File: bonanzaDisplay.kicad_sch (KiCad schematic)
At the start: 73 parts, among them J1 OLED-1.31-SSD1322, J15 SWD, J5 Conn_01x10, J6 USB_C_Receptacle_USB2.0, SW1 TS-1088-AR02016, SW2 TS-1088-AR02016, SW4 7*7*5-6P WX, U1 RP2354A, U10 TPS82130, U2 XC6206P302MR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

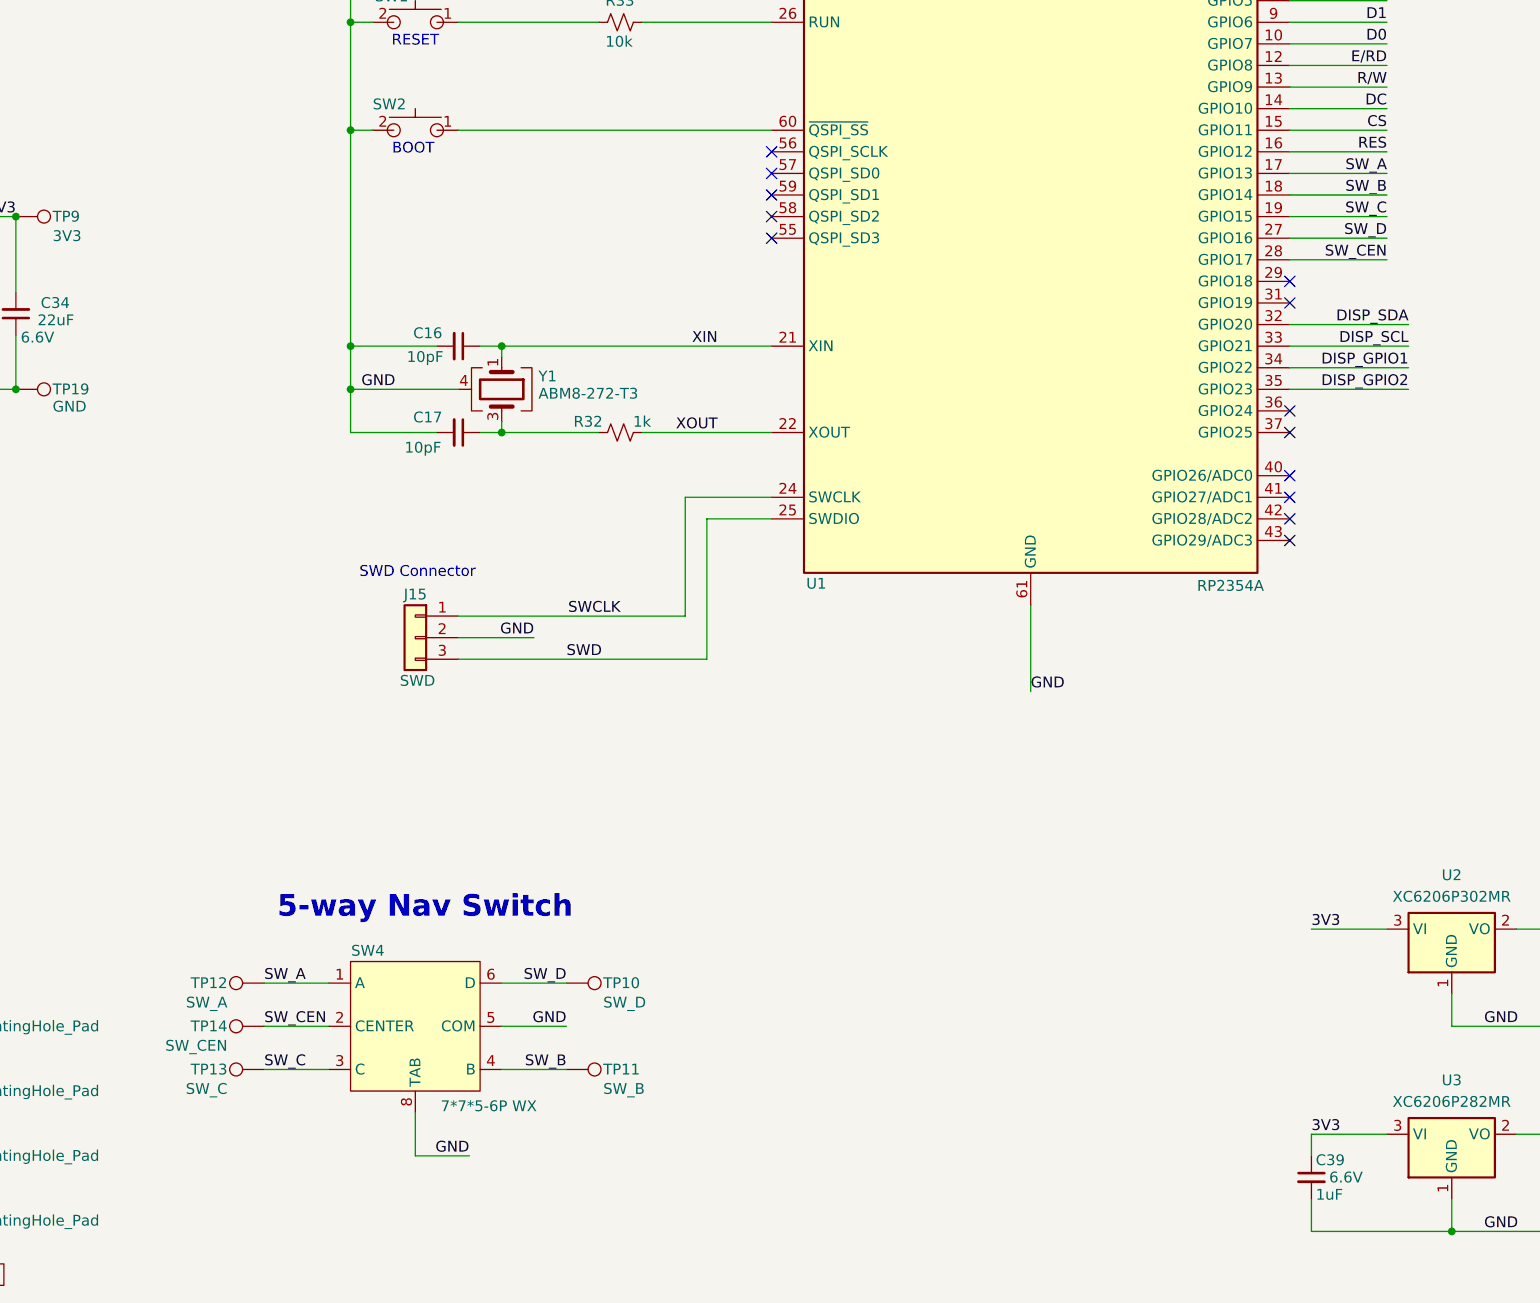
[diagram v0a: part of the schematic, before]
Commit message: switched to dial switch. added OLED 3D CAD. ordered PCBA
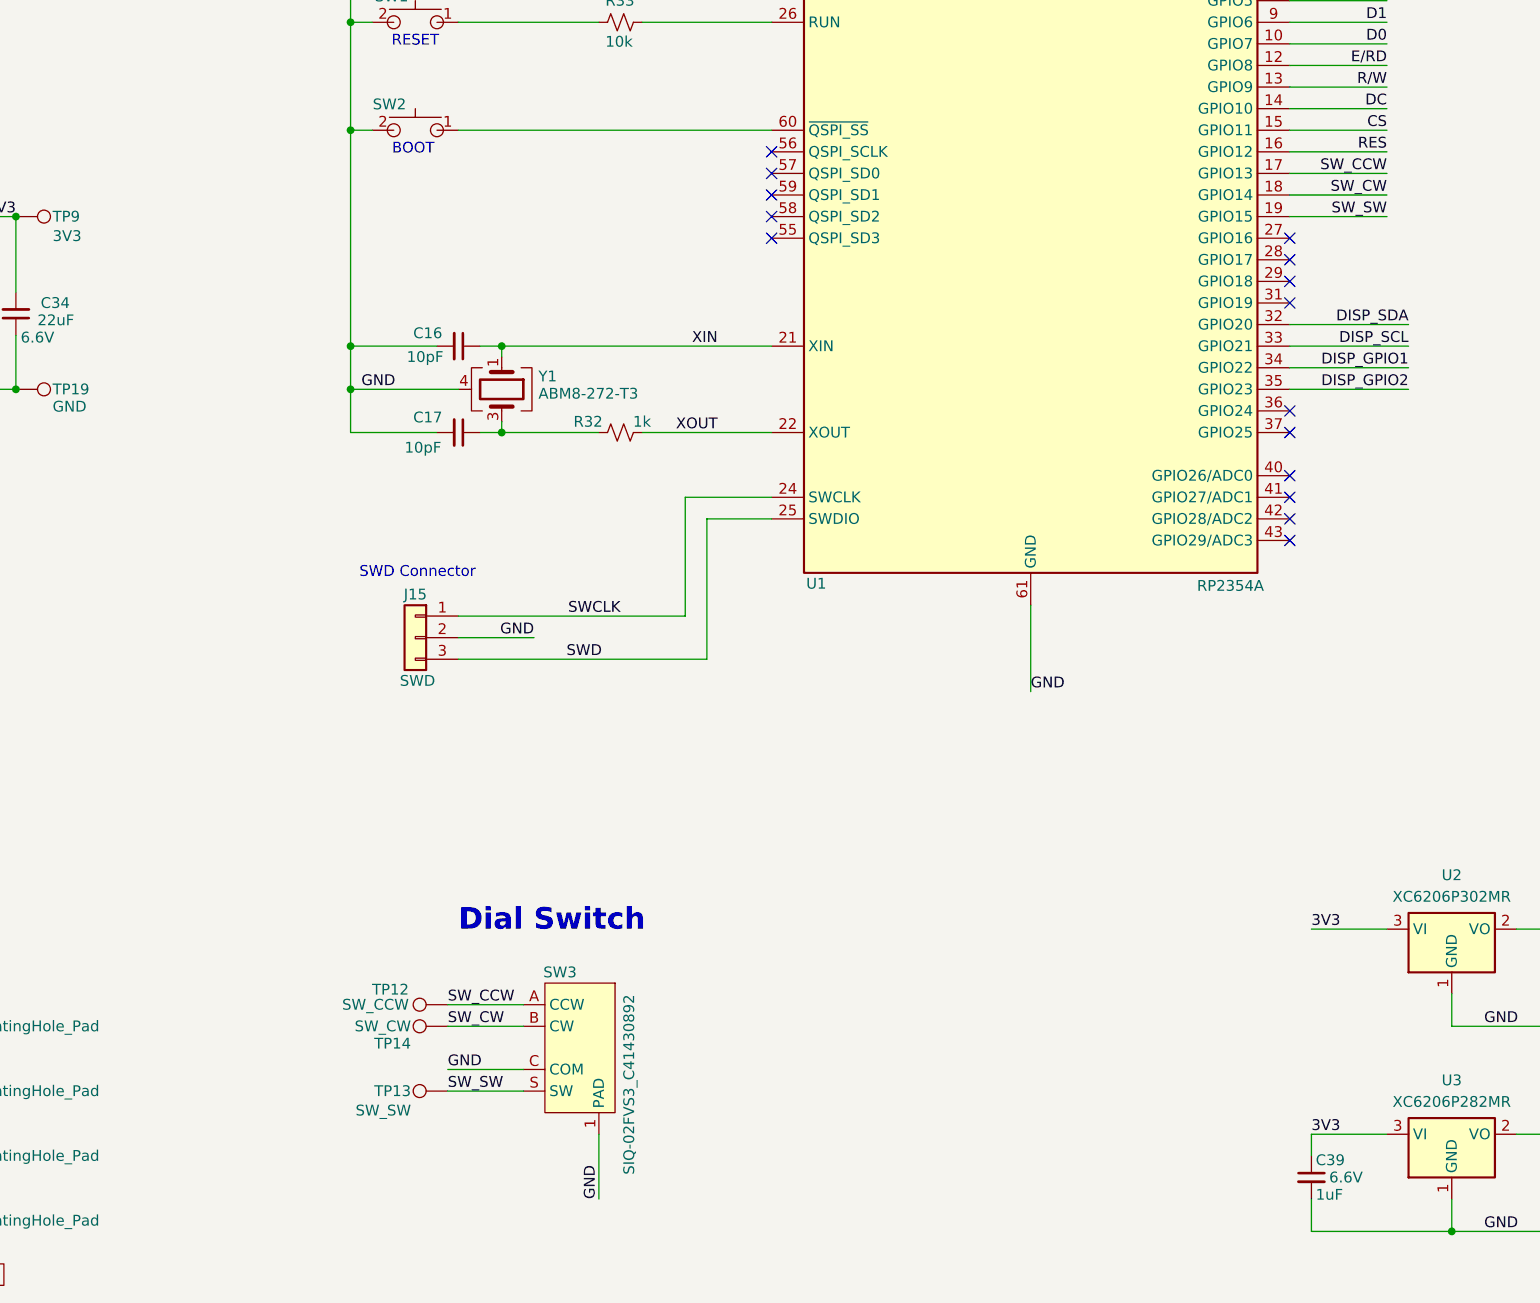
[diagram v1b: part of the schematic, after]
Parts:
- removed SW4: 7*7*5-6P WX, bonanzaDisplay:SW-SMD_6P-L7.0-W7.0-P1.40-LS7.4-TL, symbol bonanzaDisplay:tactile-switch-5way
- removed TP10: SW_D, bonanzaDisplay:TestPoint_Pad_D1.0mm, symbol Connector:TestPoint
- removed TP11: SW_B, bonanzaDisplay:TestPoint_Pad_D1.0mm, symbol Connector:TestPoint
- added SW3: SIQ-02FVS3_C41430892, bonanzaDisplay:SW-SMD_SIQ-02FVS3, symbol bonanzaDisplay:SIQ-02FVS3_C41430892
- C34: LCSC C386093 -> C12891
- R39: LCSC C137960 -> C25900
- TP12: value SW_A -> SW_CCW
- TP13: value SW_C -> SW_SW
- TP14: value SW_CEN -> SW_CW
- U10: LCSC C106235 -> C473914
- U2: LCSC C477764 -> C9972
- Y1: LCSC C171694 -> C9002
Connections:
- net GND: now also SW3.1 (PAD), SW3.2 (PAD), SW3.C (COM)
- net SW_A renamed SW_CCW
- net SW_CCW: now also SW3.A (CCW)
- net SW_B renamed SW_CW
- net SW_CW: now also TP14.1, SW3.B (CW)
- net SW_C renamed SW_SW
- net SW_SW: now also SW3.S (SW)
- net SW_CEN: no longer names the net of U1.28 (GPIO17)
- net SW_CEN: no longer TP14.1
- net SW_D: no longer names the net of U1.27 (GPIO16)
- no-connect marks 19 -> 21
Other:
- note added: "Dial Switch"
- note removed: "5-way Nav Switch"
- moved on the sheet: TP12, TP13, TP14

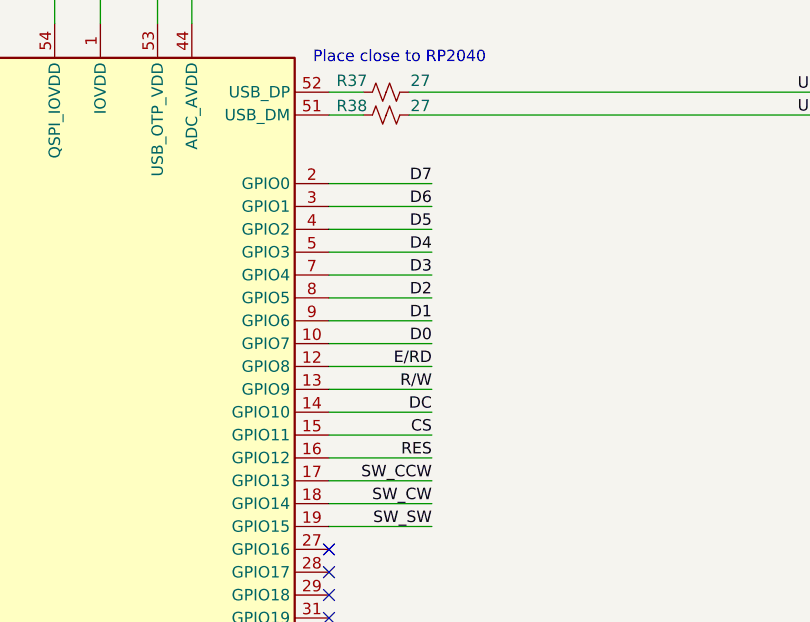
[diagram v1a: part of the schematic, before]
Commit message: fix display connector pinout for #1
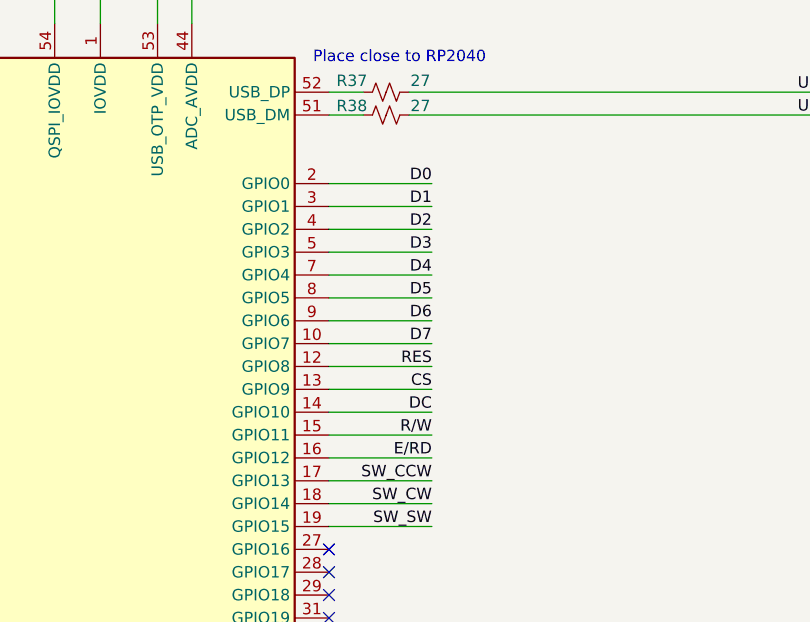
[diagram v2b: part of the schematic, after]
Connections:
- net CS: now also U1.13 (GPIO9); no longer U1.15 (GPIO11)
- net D0: now also U1.2 (GPIO0); no longer U1.10 (GPIO7)
- net D1: now also U1.3 (GPIO1); no longer U1.9 (GPIO6)
- net D2: now also U1.4 (GPIO2); no longer U1.8 (GPIO5)
- net D3: now also U1.5 (GPIO3); no longer U1.7 (GPIO4)
- net D4: now also U1.7 (GPIO4); no longer U1.5 (GPIO3)
- net D5: now also U1.8 (GPIO5); no longer U1.4 (GPIO2)
- net D6: now also U1.9 (GPIO6); no longer U1.3 (GPIO1)
- net D7: now also U1.10 (GPIO7); no longer U1.2 (GPIO0)
- net E/RD: now also U1.16 (GPIO12); no longer U1.12 (GPIO8)
- net RES: now also U1.12 (GPIO8); no longer U1.16 (GPIO12)
- net R/W: now also U1.15 (GPIO11); no longer U1.13 (GPIO9)

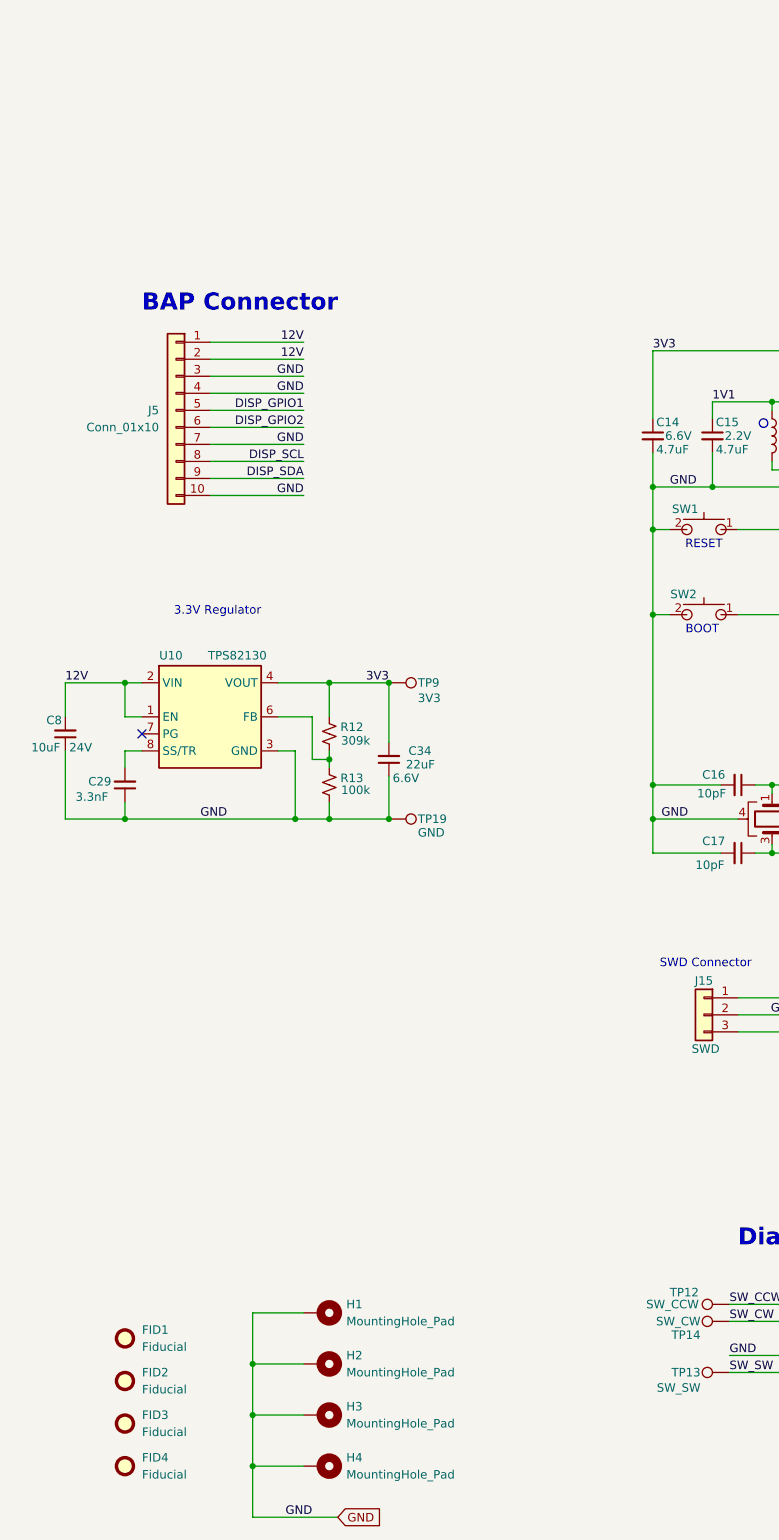
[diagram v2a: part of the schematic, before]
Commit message: switched 10pin FFC connector to right angle. made PCB shorter. most routing done.
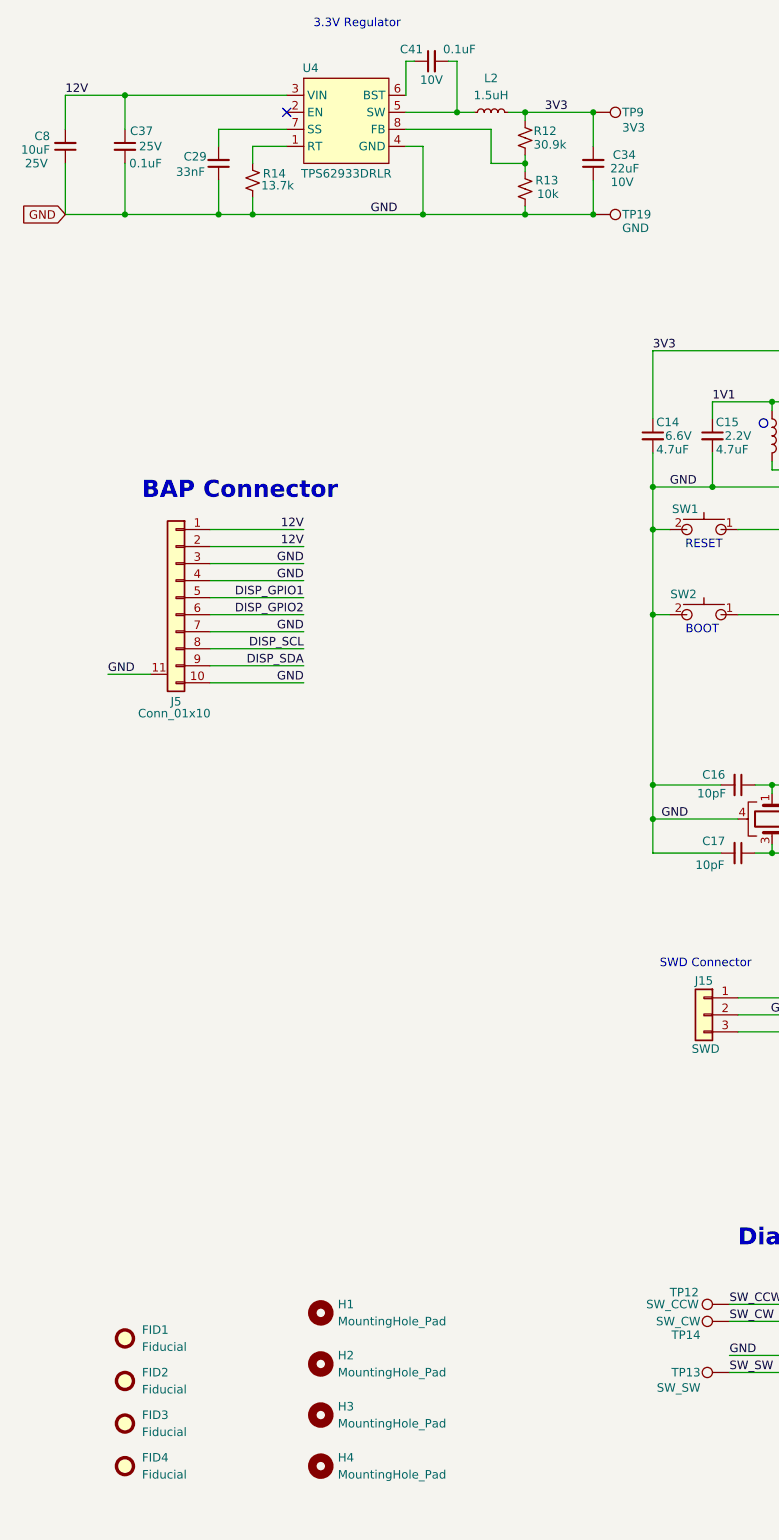
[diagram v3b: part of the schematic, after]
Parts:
- removed U10: TPS82130, bonanzaDisplay:Texas_SIL0008D_MicroSiP-8-1EP_2.8x3mm_P0.65mm_EP1.1x1.9mm_ThermalVias, symbol bonanzaDisplay:TPS82130
- added C37, C41: 0.1uF, Capacitor_SMD:C_0402_1005Metric, symbol Device:C_Small
- added L2: 1.5uH, bonanzaDisplay:IND-SMD_L2.0-W1.6, symbol Device:L_Small
- added R14: 13.7k, Resistor_SMD:R_0402_1005Metric, symbol Device:R_Small_US
- added U4: TPS62933DRLR, bonanzaDisplay:SOT-583-8_L2.1-W1.2-P0.50-LS1.6-BR, symbol bonanzaDisplay:TPS62933DRLR
- C29: value 3.3nF -> 33nF; DK 1276-CL05B332KA5VPNCCT-ND -> (none); LCSC C307337 -> (none); PARTNO CL05B332KA5VPNC -> (none)
- C34: footprint Capacitor_SMD:C_1206_3216Metric -> Capacitor_SMD:C_0805_2012Metric; DK 587-3246-1-ND -> (none); LCSC C12891 -> (none); PARTNO TMK316BBJ226ML-T -> MSASL219LB5226MTNA01; Voltage 6.6V -> 10V
- C8: footprint Capacitor_SMD:C_0603_1608Metric -> Capacitor_SMD:C_0805_2012Metric; DK 490-18214-1-ND -> (none); LCSC C344022 -> (none); PARTNO GRM188R61E106KA73D -> MSAST21GBB5106MTNA01; Voltage 24V -> 25V
- H1, H2, H3, H4: footprint MountingHole:MountingHole_3.2mm_M3_Pad_Via -> MountingHole:MountingHole_3.2mm_M3; symbol Mechanical:MountingHole_Pad -> Mechanical:MountingHole
- J5: footprint bonanzaDisplay:CONN10_1-1735042-0 -> bonanzaDisplay:FPC-SMD_10P-P1.0_FGS-XJ-H2.0; symbol Connector_Generic:Conn_01x10 -> bonanzaDisplay:FPC-SMD_10P-P1.0_FGS-XJ-H2.0; DK A117817CT-ND -> (none); LCSC C2908569 -> C262756; PARTNO 1-1735042-0 -> AFA01-S10FCA-00
- R12: value 309k -> 30.9k; LCSC C171694 -> (none)
- R13: value 100k -> 10k; DK 311-100KLRCT-ND -> (none); LCSC C60491 -> (none); PARTNO RC0402FR-07100KL -> (none)
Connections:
- net 12V: now also C37.1, U4.3 (VIN)
- net 3V3: now also L2.2
- net GND: now also J5.11, J5.12, C37.2, R14.1, U4.4 (GND); no longer H1.1, H2.1, H3.1, H4.1
- net at R12.1, R13.2: now also U4.8 (FB)
- net at C29.2: now also U4.7 (SS)
- new net: R14.2, U4.1 (RT)
- new net: C41.2, L2.1, U4.5 (SW)
- new net: C41.1, U4.6 (BST)
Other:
- moved on the sheet: C29, C34, C8, R12, R13, TP19, TP9

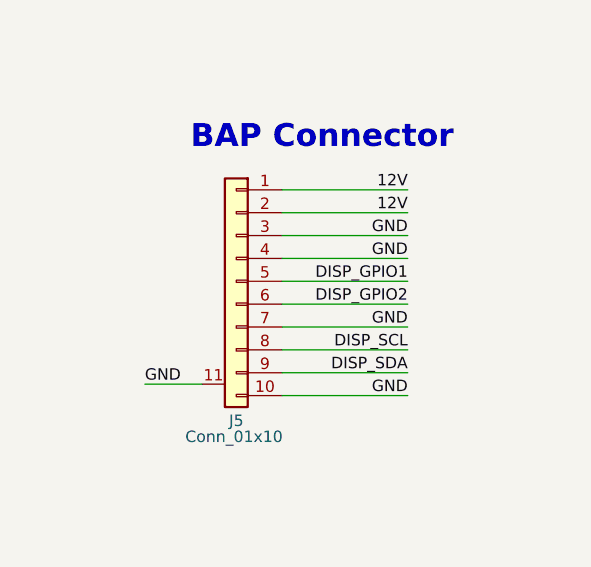
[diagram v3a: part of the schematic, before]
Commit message: cleanup footprints
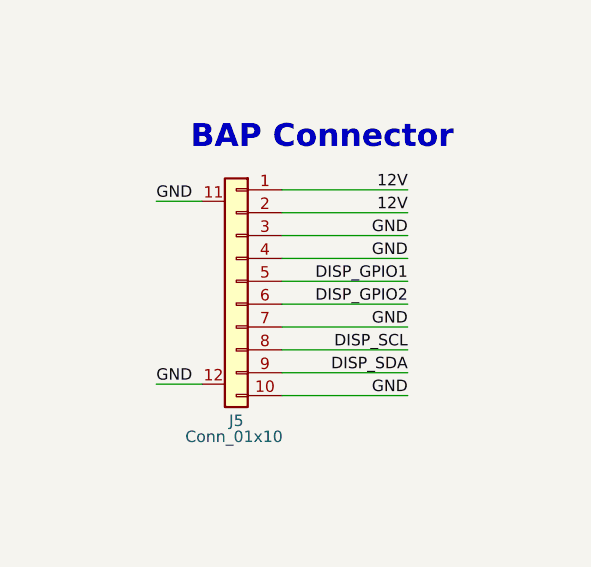
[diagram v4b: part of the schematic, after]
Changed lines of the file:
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@@
 	(wire
 		(pts
-			(xy 41.91 130.81) (xy 48.26 130.81)
+			(xy 43.18 130.81) (xy 48.26 130.81)
 		)
 		(stroke
@@
 		(pts
 			(xy 172.72 69.85) (xy 163.83 69.85)
+		)
+		(stroke
+			(width 0)
+			(type default)
+		)
+	)
+	(wire
+		(pts
+			(xy 43.18 110.49) (xy 48.26 110.49)
 		)
 		(stroke
@@
 	)
 	(label "GND"
-		(at 41.91 130.81 0)
+		(at 43.18 130.81 0)
 		(effects
 			(font
@@
 		(effects
 			(font
+				(size 1.27 1.27)
+			)
+			(justify left bottom)
+		)
+	)
+	(label "GND"
+		(at 43.18 110.49 0)
+		(effects
+			(font
